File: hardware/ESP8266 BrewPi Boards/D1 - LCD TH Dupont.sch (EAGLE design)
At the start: 13 parts, among them J1 RJ11-4L-B, Q1 BSS123, Q2 BSS123

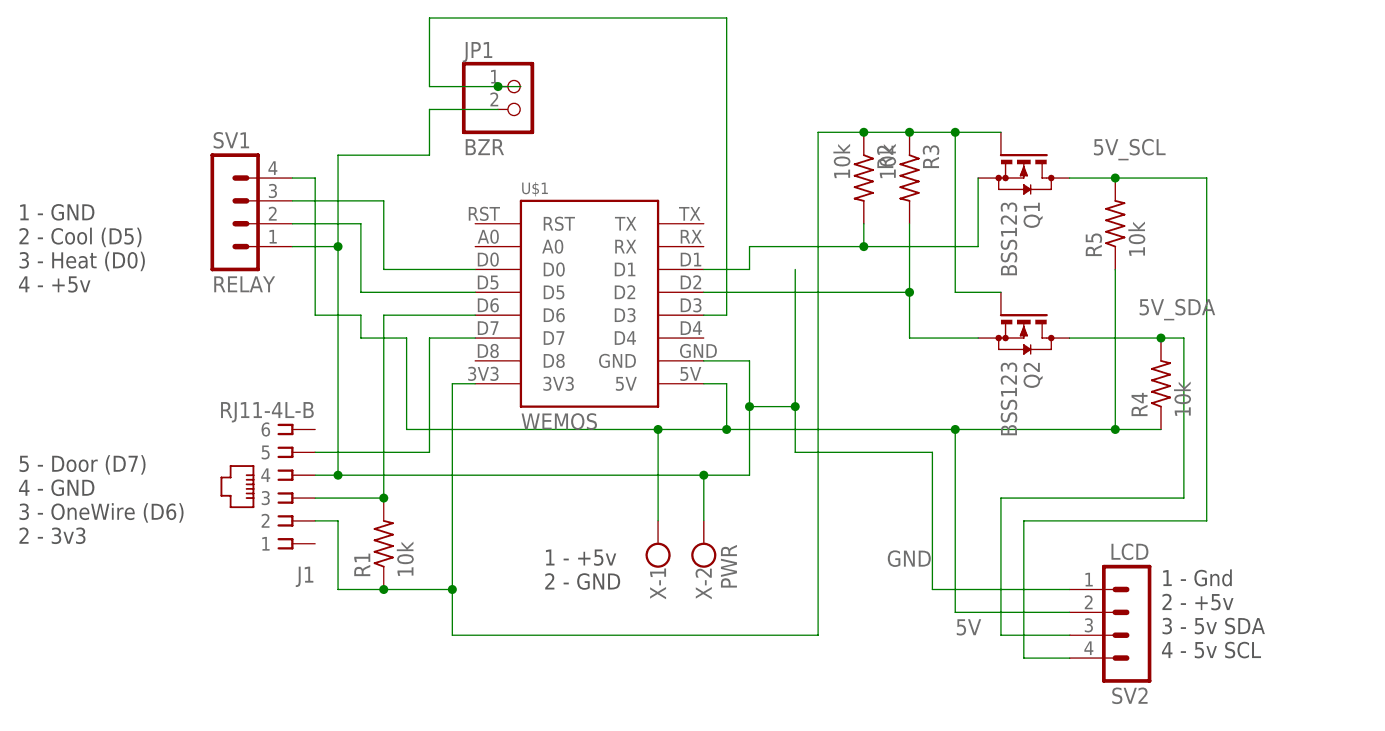
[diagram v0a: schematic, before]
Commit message: Updating docs & adding new eagle schematics
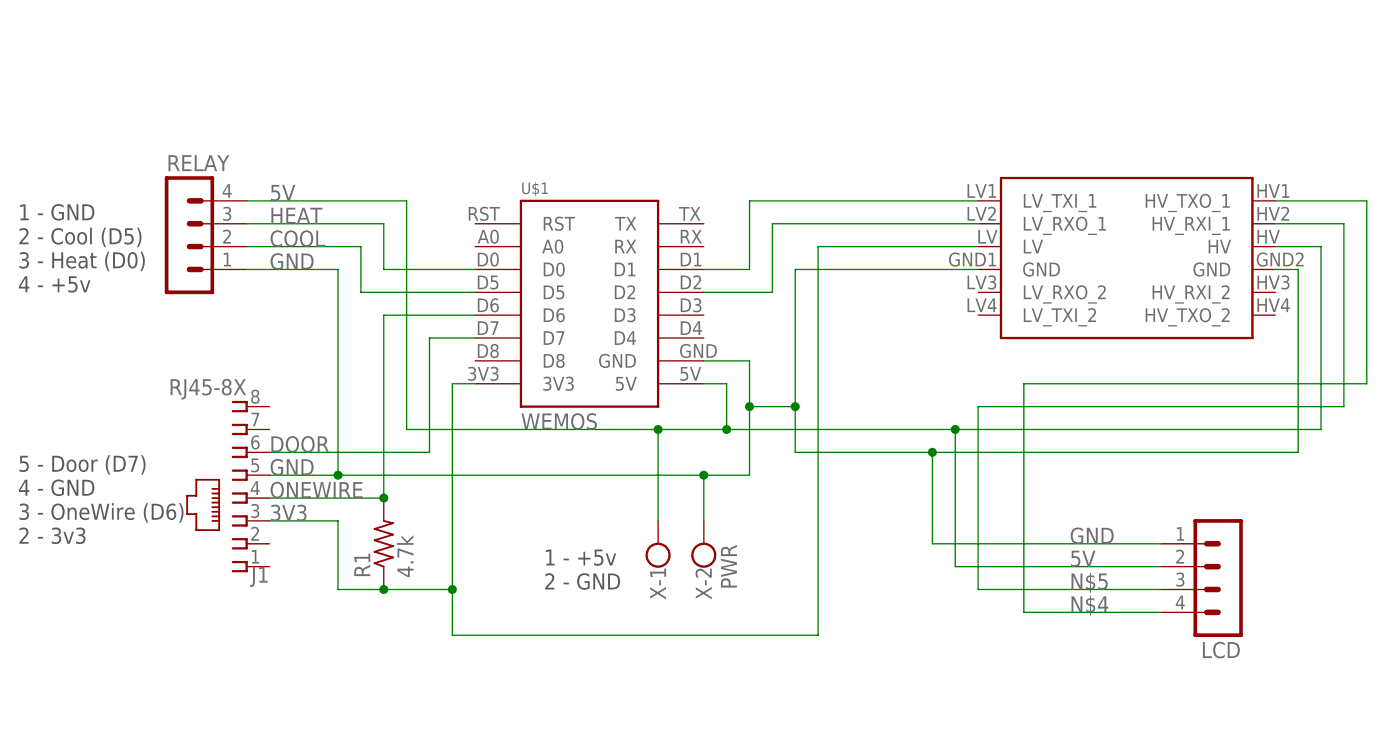
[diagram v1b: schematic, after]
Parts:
- removed JP1: BZR, pinhead:PINHD-1X2
- removed Q1, Q2: BSS123, transistor-small-signal:BSS123
- removed R2, R3, R4, R5: 10k, rcl:R-US_R0805
- removed SV1: RELAY, con-lstb:MA04-1
- removed SV2: LCD, con-lstb:MA04-1
- added LCD, RELAY: (no value), con-lstb:MA04-1
- added U$3: SPARKFUN_LOGIC_LEVEL_CONVERTER, SparkFun-Boards:SPARKFUN_LOGIC_LEVEL_CONVERTER
- J1: value RJ11-4L-B -> RJ45-8X; device con-tycoelectronics:RJ11-4L-B -> con-tycoelectronics:RJ45-8X
- R1: value 10k -> 4.7k; device rcl:R-US_R0805 -> rcl:R-US_0309/12
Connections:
- removed net 3V3_SCL: Q1.S, R2.2, U$1.D1
- removed net 3V3_SDA: Q2.S, R3.2, U$1.D2
- removed net 5V_SCL: Q1.D, R5.2, SV2.4
- removed net 5V_SDA: Q2.D, R4.2, SV2.3
- removed net D6: J1.3, R1.2, U$1.D6
- removed net D7: J1.5, U$1.D7
- removed net N$3: J1.2, Q1.G, Q2.G, R1.1, R2.1, R3.1, U$1.3V3
- removed net N$6: JP1.1, U$1.D3
- removed net N$7: SV1.2, U$1.D5
- removed net N$8: SV1.3, U$1.D0
- new net 3V3: J1.3, R1.1, U$1.3V3, U$3.LV
- new net COOL: RELAY.2, U$1.D5
- new net DOOR: J1.6, U$1.D7
- new net HEAT: RELAY.3, U$1.D0
- new net N$1: U$1.D1, U$3.LV_TXI_1
- new net N$2: U$1.D2, U$3.LV_RXO_1
- new net N$4: LCD.4, U$3.HV_TXO_1
- new net N$5: LCD.3, U$3.HV_RXI_1
- new net ONEWIRE: J1.4, R1.2, U$1.D6
- net 5V: now also LCD.2, RELAY.4, U$3.HV; no longer R4.1, R5.1, SV1.4, SV2.2
- net GND: now also J1.5, LCD.1, RELAY.1, U$3.GND, U$3.GND@2; no longer J1.4, JP1.2, SV1.1, SV2.1
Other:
- note removed: "1 - Gnd 2 - +5v 3 - 5v SDA 4 - 5v SCL"
